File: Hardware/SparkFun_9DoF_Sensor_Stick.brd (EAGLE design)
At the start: 34.3 x 10.2 mm, 27 parts, among them U1 ITG-32001:1, U2 ADXL345, U4 3.3V

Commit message: Mid revision work - NOT FUNCTIONAL
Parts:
- removed C12: 4.7uF, SparkFun:0402-CAP
- removed LED1: Blue, SparkFun:LED-0603
- removed U$1: CREATIVE_COMMONS, SparkFun:CREATIVE_COMMONS
- removed U$2: HMC5883L1:1, Testing:16LPCC_1:1
- added C13: 10uF, SparkFun-Capacitors:EIA3216
- added D1: RED, SparkFun-LED:LED-0603
- added FRAME1: (no value), SparkFun-Aesthetics:CREATIVE_COMMONS
- added SJ1: JUMPER-PAD-3-NC_BY_PASTE, SparkFun-Passives:PAD-JUMPER-3-NC_BY_PASTE_YES_SILK_FULL_BOX
- added SJ2, SJ3, SJ4: JUMPER-PAD-2-NC_BY_TRACE, SparkFun-Passives:PAD-JUMPER-2-NC_BY_TRACE_YES_SILK
- added U$4: REVISION, SparkFun-Aesthetics:REVISION
- added U3: 3.3V/150mA, SparkFun-PowerIC:SOT23-5
- C1, C10, C11, C2, C3, C4, C5, C6, C7, C8, C9: device SparkFun:0402-CAP -> SparkFun-Capacitors:0603-CAP
- JP1, JP2: device SparkFun:FIDUCIAL-1X2 -> SparkFun-Aesthetics:FIDUCIAL-1X2
- JP3: device SparkFun:1X04 -> SparkFun-Connectors:1X04
- JP4: value LOGO-SFESK -> SFE_LOGO_FLAME.1_INCH; device SparkFun:SFE-LOGO-FLAME -> SparkFun-Aesthetics:SFE_LOGO_FLAME_.1
- JP5: device SparkFun:STAND-OFF -> SparkFun-Electromechanical:STAND-OFF
- R1, R2, R3: device SparkFun:0402-RES -> SparkFun-Resistors:0603-RES
- U$3: device SparkFun:OSHW-LOGO-S -> SparkFun-Aesthetics:OSHW-LOGO-S
- U1: device Testing:QFN-24_1:1 -> SparkFun-Sensors:QFN-24_ITG3200_1:1
- U2: value ADXL345 -> ADXL345"; device SparkFun:LGA14 -> SparkFun-Sensors:ADXL3451:1
- U4: value 3.3V -> HMC5883LSMD; device SparkFun:SOT23-5 -> SparkFun-Sensors:16LPCC
- moved U4 10.2 mm to (16.5, 5.08), turned to 270 degrees
- moved JP3 7.62 mm to (1.27, 1.27), turned to 90 degrees
- moved C9 5.71 mm to (29.8, 1.27), turned to 0 degrees
- moved JP2 5.54 mm to (-1.02, -1.08)
- moved R3 5.40 mm to (25.7, 1.27)
- moved R1 5.40 mm to (3.81, 6.03), turned to 90 degrees
- moved U$3 4.02 mm to (31.1, 12.1)
- moved JP4 3.93 mm to (31.9, 0.19)
- moved C6 3.81 mm to (27.9, 8.89), turned to 180 degrees
- moved C7 3.17 mm to (20.3, 1.91), turned to 270 degrees
- moved C2 2.54 mm to (12.7, 8.89)
- moved C3 1.90 mm to (17.1, 1.27)
- moved C4 1.03 mm to (14.0, 1.27), turned to 0 degrees
- moved C11 0.95 mm to (3.81, 2.86), turned to 270 degrees
- moved C10 0.64 mm to (6.99, 8.89), turned to 180 degrees
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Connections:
- new net N$10: SJ2.2, U2.12
- new net N$12: C5.1, SJ4.2, U4.13, U4.2, U4.4
- new net N$6: R1.2, SJ1.3
- new net N$8: R2.2, SJ1.1
- new net N$9: SJ3.2, U1.9
- net 3.3V: now also C13.A, D1.A, SJ1.2, SJ4.1, U3.5; no longer C12.1, C5.1, LED1.A, R1.2, R2.2, U$2.13, U$2.2, U$2.4, U4.5
- net GND: now also C13.C, JP3.1, SJ2.1, SJ3.1, U3.2, U4.11, U4.9; no longer C12.2, JP3.3, U$2.11, U$2.9, U1.9, U2.12, U4.2
- net N$1: now also U4.10; no longer U$2.10
- net N$2: now also U4.8; no longer U$2.8
- net N$3: now also U4.12; no longer U$2.12
- net N$4: now also D1.C; no longer LED1.C
- net SCL: now also JP3.4, U4.1; no longer JP3.1, U$2.1
- net SDA: now also JP3.3, U4.16; no longer JP3.2, U$2.16
- net VCC: now also JP3.2, U3.1, U3.3; no longer JP3.4, U4.1, U4.3
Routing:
- net 3.3V: track 82.9 -> 67.0 mm
- net N$12: track 0.00 -> 9.86 mm, vias 0 -> 1
- net N$9: track 0.00 -> 6.12 mm, vias 0 -> 1
- net N$5: track 1.93 -> 6.49 mm
- net SDA: track 39.1 -> 41.2 mm
- net SCL: track 42.7 -> 40.9 mm
- net N$7: track 1.90 -> 3.58 mm
- net N$3: track 10.7 -> 9.15 mm
- net VCC: track 9.19 -> 7.78 mm
- net N$2: track 2.90 -> 4.27 mm
- net N$1: track 3.53 -> 2.45 mm
- net GND: track 32.5 -> 31.8 mm
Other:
- board text added: "Toni Klopfenstein"
- board text added: "v16"
- board text removed: "v15"

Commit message: Mid layout attempt
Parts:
- moved SJ1 7.85 mm to (3.81, 6.99), flipped to the bottom
- moved JP2 4.60 mm to (3.17, 0.83)
- moved C13 3.55 mm to (6.35, 1.91)
- moved C3 1.61 mm to (18.8, 1.32)
- moved C4 1.53 mm to (14.0, 2.80), turned to 270 degrees
- moved R1 1.43 mm to (4.47, 7.30), turned to 0 degrees
- moved C1 1.20 mm to (13.9, 6.08)
- moved C11 1.14 mm to (3.17, 3.81)
- moved C5 0.66 mm to (18.1, 8.94)
- moved C8 0.66 mm to (24.8, 8.94)
- moved U1 0.66 mm to (24.8, 5.13)
- moved C2 0.66 mm to (13.4, 8.94)
- moved C7 0.66 mm to (21.0, 1.96)
- moved D1 0.66 mm to (23.5, 1.32)
- moved R3 0.66 mm to (26.4, 1.32)
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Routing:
- net GND: track 31.8 -> 20.7 mm, vias 7 -> 5
- net SCL: track 40.9 -> 44.2 mm
- net SDA: track 41.2 -> 38.5 mm, vias 3 -> 2
- net N$2: track 4.27 -> 2.08 mm
- net N$1: track 2.45 -> 3.39 mm

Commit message: Complete reroute-WIP
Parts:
- moved C10 15.6 mm to (22.8, 5.42), turned to 270 degrees
- moved C4 15.5 mm to (29.5, 1.22), turned to 180 degrees
- moved D1 13.0 mm to (10.8, -1.22)
- moved R3 12.1 mm to (14.6, -1.32), turned to 0 degrees
- moved C9 11.5 mm to (21.6, 9.21), turned to 180 degrees
- moved C6 11.3 mm to (20.3, 1.22)
- moved SJ3 10.7 mm to (16.2, 8.86), flipped to the top, turned to 180 degrees
- moved C5 10.1 mm to (28.2, 8.89)
- moved U4 9.21 mm to (26.4, 5.13)
- moved SJ4 8.62 mm to (25.0, 8.76), flipped to the top, turned to 0 degrees
- moved JP4 7.63 mm to (29.7, -7.11)
- moved C3 7.25 mm to (26.0, 1.32), turned to 180 degrees
- moved C7 6.65 mm to (14.3, 1.56), turned to 180 degrees
- moved U1 6.35 mm to (18.4, 5.13)
- moved C1 4.44 mm to (10.4, 8.89), turned to 180 degrees
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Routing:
- net 3.3V: track 67.5 -> 39.6 mm, vias 4 -> 3
- net GND: track 20.7 -> 5.19 mm, vias 5 -> 0
- net SCL: track 44.2 -> 32.2 mm, vias 3 -> 1
- net SDA: track 38.5 -> 31.0 mm, vias 2 -> 1
- net N$2: track 2.08 -> 8.87 mm, vias 0 -> 2
- net N$3: track 8.77 -> 3.51 mm, vias 2 -> 0
- net N$8: track 0.00 -> 2.08 mm
- net N$6: track 0.00 -> 2.04 mm
- net N$5: track 6.49 -> 4.47 mm
- net N$9: track 6.12 -> 4.62 mm, vias 1 -> 0
- net N$4: track 1.13 -> 0.00 mm
- net N$12: track 9.86 -> 9.04 mm, vias 1 -> 0
- net N$1: track 3.39 -> 2.77 mm
- net N$7: track 3.58 -> 4.20 mm

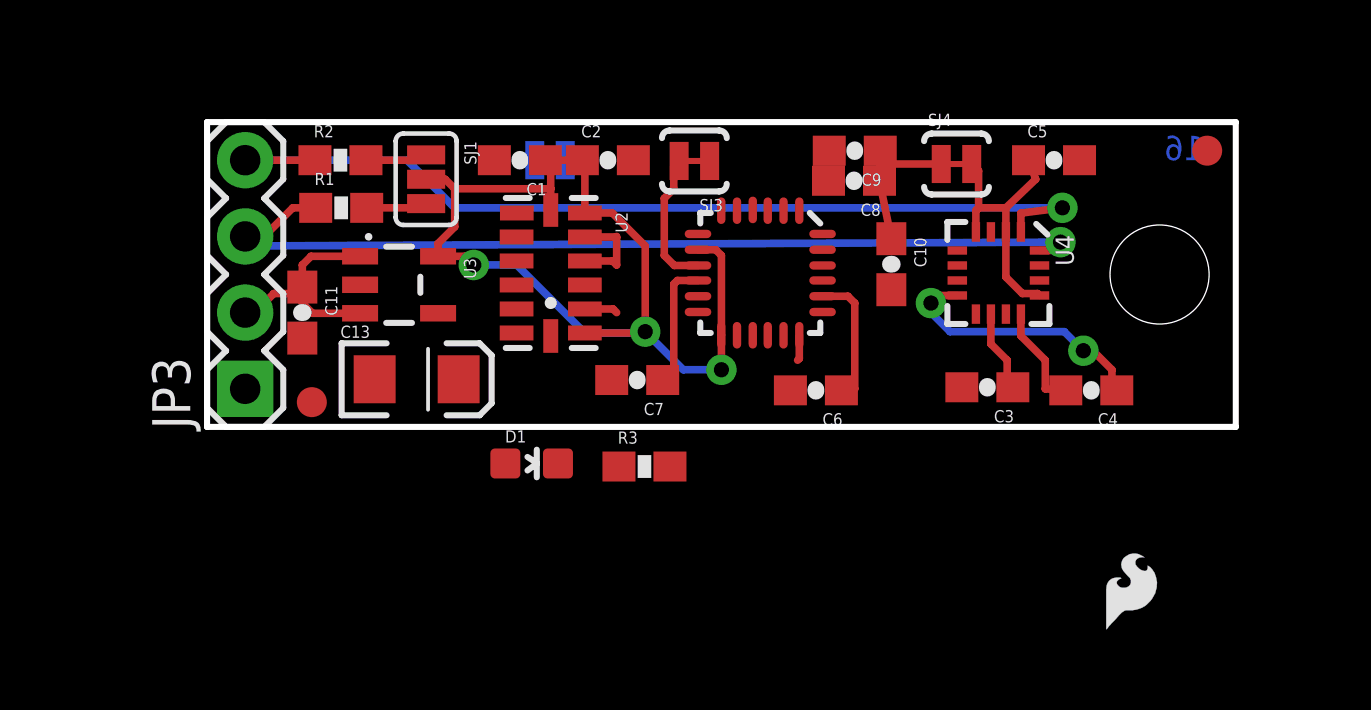
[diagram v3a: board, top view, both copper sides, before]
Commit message: horizontal orientation
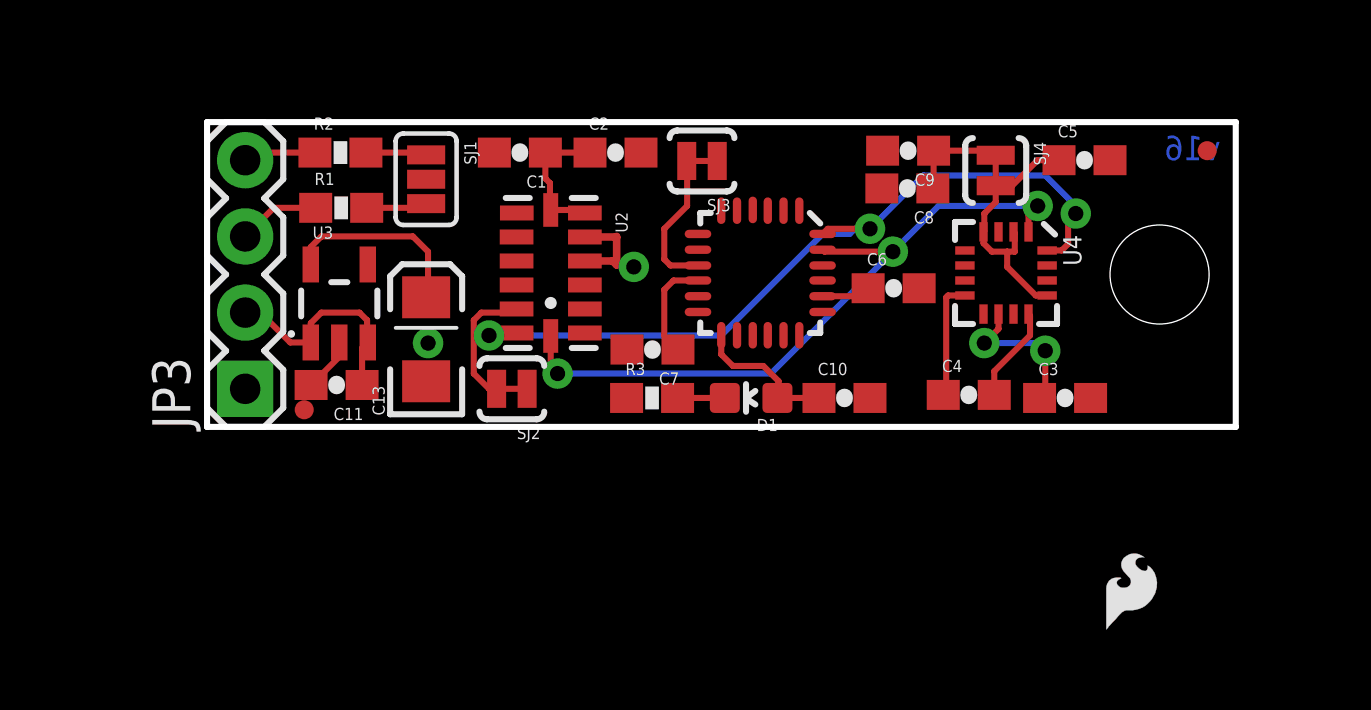
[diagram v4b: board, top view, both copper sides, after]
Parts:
- JP1, JP2: value FIDUCIAL1X2 -> FIDUCIALUFIDUCIAL; device SparkFun-Aesthetics:FIDUCIAL-1X2 -> SparkFun-Aesthetics:MICRO-FIDUCIAL
- moved SJ2 7.73 mm to (10.2, 1.27), flipped to the top, turned to 180 degrees
- moved D1 7.63 mm to (18.1, 0.97), turned to 90 degrees
- moved C10 4.72 mm to (21.2, 0.97), turned to 0 degrees
- moved C6 4.28 mm to (22.9, 4.62), turned to 0 degrees
- moved C4 4.09 mm to (25.4, 1.07), turned to 0 degrees
- moved C11 2.67 mm to (4.32, 1.40), turned to 180 degrees
- moved C3 2.62 mm to (28.6, 0.97), turned to 0 degrees
- moved R3 2.30 mm to (14.8, 0.97)
- moved U3 2.09 mm to (4.41, 4.11), turned to 0 degrees
- moved C8 1.80 mm to (23.3, 7.95)
- moved C9 1.78 mm to (23.4, 9.21)
- moved C13 1.37 mm to (7.30, 2.92), turned to 90 degrees
- moved SJ4 1.33 mm to (26.3, 8.55), turned to 270 degrees
- moved C7 1.14 mm to (14.8, 2.58)
- moved C5 1.02 mm to (29.2, 8.89)
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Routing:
- net 3.3V: track 39.6 -> 19.3 mm, vias 3 -> 0
- net SCL: track 32.2 -> 25.5 mm, vias 1 -> 3
- net N$2: track 8.87 -> 3.94 mm, vias 2 -> 0
- net N$10: track 0.00 -> 4.33 mm
- net N$5: track 4.47 -> 1.63 mm
- net N$1: track 2.77 -> 4.95 mm, vias 0 -> 2
- net N$4: track 0.00 -> 1.58 mm
- net SDA: track 31.0 -> 29.7 mm, vias 1 -> 3
- net N$7: track 4.20 -> 3.44 mm
- net GND: track 5.19 -> 4.93 mm, vias 0 -> 2

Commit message: No airwires!
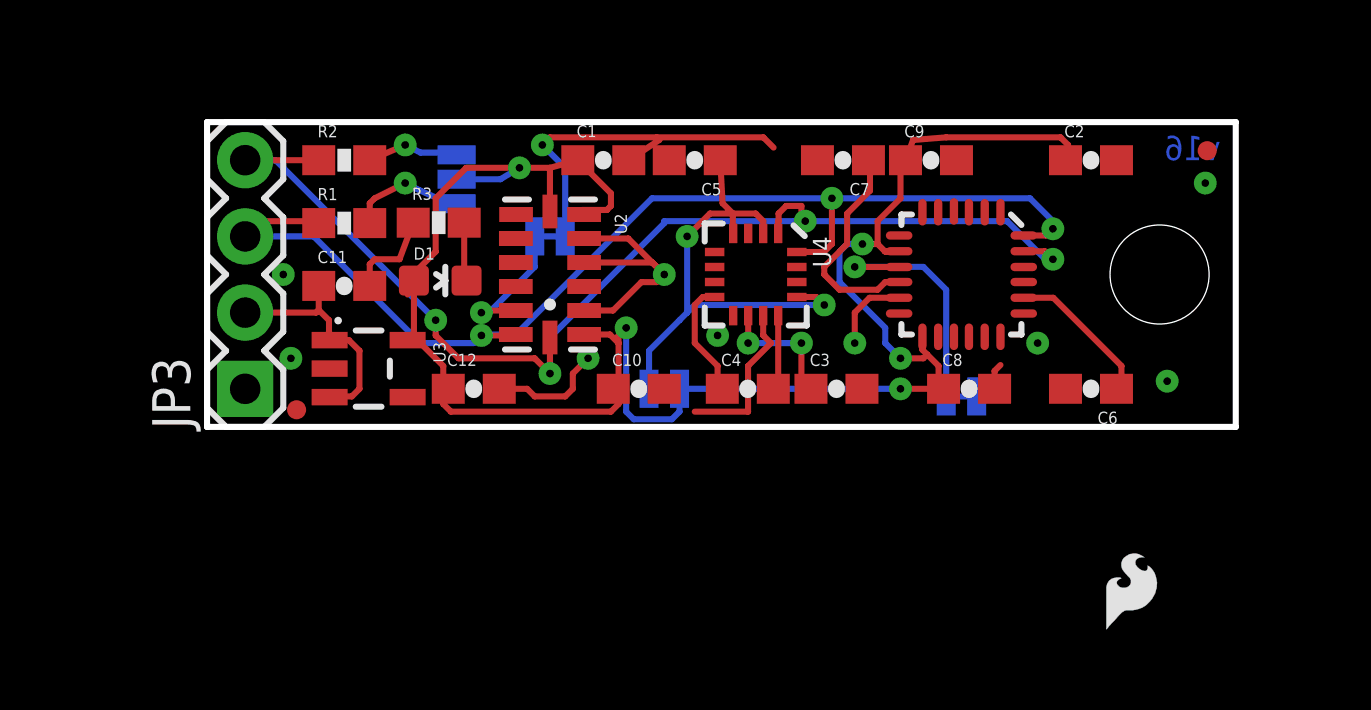
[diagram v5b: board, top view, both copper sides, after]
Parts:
- removed C13: 10uF, SparkFun-Capacitors:EIA3216
- added C12: 10uF, SparkFun-Capacitors:0603-CAP
- moved C2 15.9 mm to (29.5, 8.89)
- moved SJ4 13.2 mm to (15.2, 1.27), flipped to the bottom, turned to 0 degrees
- moved C5 13.0 mm to (16.3, 8.89), turned to 180 degrees
- moved SJ3 11.7 mm to (25.1, 1.02), flipped to the bottom, turned to 0 degrees
- moved D1 11.1 mm to (7.77, 4.88), turned to 270 degrees
- moved R3 9.20 mm to (7.72, 6.81)
- moved C7 8.95 mm to (21.2, 8.89)
- moved U4 8.34 mm to (18.3, 5.08)
- moved C3 7.63 mm to (21.0, 1.27)
- moved C6 7.38 mm to (29.5, 1.27), turned to 180 degrees
- moved C4 7.37 mm to (18.0, 1.27)
- moved C8 6.99 mm to (25.4, 1.27), turned to 0 degrees
- moved C10 6.86 mm to (14.4, 1.27)
- moved U1 6.71 mm to (25.1, 5.08)
- moved SJ2 5.24 mm to (11.4, 6.35), flipped to the bottom, turned to 0 degrees
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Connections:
- net 3.3V: now also C12.1; no longer C13.A
- net GND: now also C12.2; no longer C13.C
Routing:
- net 3.3V: track 19.3 -> 65.2 mm, vias 0 -> 5
- net GND: track 4.93 -> 37.8 mm, vias 2 -> 10
- net SCL: track 25.5 -> 40.8 mm, vias 3 -> 4
- net SDA: track 29.7 -> 38.8 mm
- net N$12: track 8.62 -> 17.3 mm, vias 0 -> 2
- net N$7: track 3.44 -> 7.28 mm
- net N$9: track 4.81 -> 8.40 mm, vias 0 -> 1
- net N$5: track 1.63 -> 5.03 mm
- net N$6: track 2.04 -> 3.95 mm, vias 0 -> 1
- net N$8: track 2.04 -> 3.09 mm, vias 0 -> 1
- net N$4: track 1.58 -> 2.30 mm
- net N$3: track 3.21 -> 2.51 mm
- net N$1: track 4.95 -> 4.44 mm
- net N$10: track 4.33 -> 4.60 mm, vias 0 -> 1

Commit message: BOARD PROTO LAYOUT
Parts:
- moved JP2 30.6 mm to (33.6, 0.73)
- moved JP1 30.2 mm to (3.14, 9.43)
- moved U$3 27.7 mm to (8.48, 1.75)
- moved C2 24.6 mm to (4.94, 6.48), turned to 180 degrees
- moved R1 24.2 mm to (28.7, 8.89)
- moved C9 17.3 mm to (8.53, 1.47)
- moved R2 16.9 mm to (21.5, 8.89), turned to 180 degrees
- moved SJ1 16.6 mm to (24.9, 9.08), turned to 180 degrees
- moved C5 16.3 mm to (30.7, 1.47), turned to 0 degrees
- moved JP4 14.3 mm to (31.9, 6.99)
- moved C8 12.2 mm to (15.6, 8.51)
- moved SJ4 9.29 mm to (24.3, 3.37), turned to 180 degrees
- moved SJ3 9.00 mm to (17.1, 5.14)
- moved C6 8.80 mm to (20.7, 1.47)
- moved U4 8.51 mm to (26.8, 5.08)
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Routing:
- net GND: track 37.8 -> 17.4 mm, vias 10 -> 8
- net SCL: track 40.8 -> 48.2 mm, vias 4 -> 3
- net N$3: track 2.51 -> 9.19 mm, vias 0 -> 2
- net N$9: track 8.40 -> 3.89 mm
- net N$8: track 3.09 -> 6.68 mm
- net N$2: track 3.95 -> 1.23 mm
- net N$6: track 3.95 -> 6.54 mm
- net 3.3V: track 65.2 -> 67.8 mm
- net N$7: track 7.28 -> 4.88 mm
- net N$1: track 4.44 -> 2.36 mm, vias 2 -> 0
- net SDA: track 38.8 -> 40.5 mm
- net N$5: track 5.03 -> 3.65 mm
- net N$12: track 17.3 -> 16.1 mm
- net VCC: track 7.97 -> 8.99 mm
- net N$4: track 2.30 -> 1.41 mm
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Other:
- board text added: "ACL"
- board text added: "ADD."
- board text added: "I2C"
- board text added: "MAG"
- board text added: "P/U"
